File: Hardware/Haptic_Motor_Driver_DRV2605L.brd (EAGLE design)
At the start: 20.3 x 21.6 mm, 15 parts, among them U1 DRV2605L

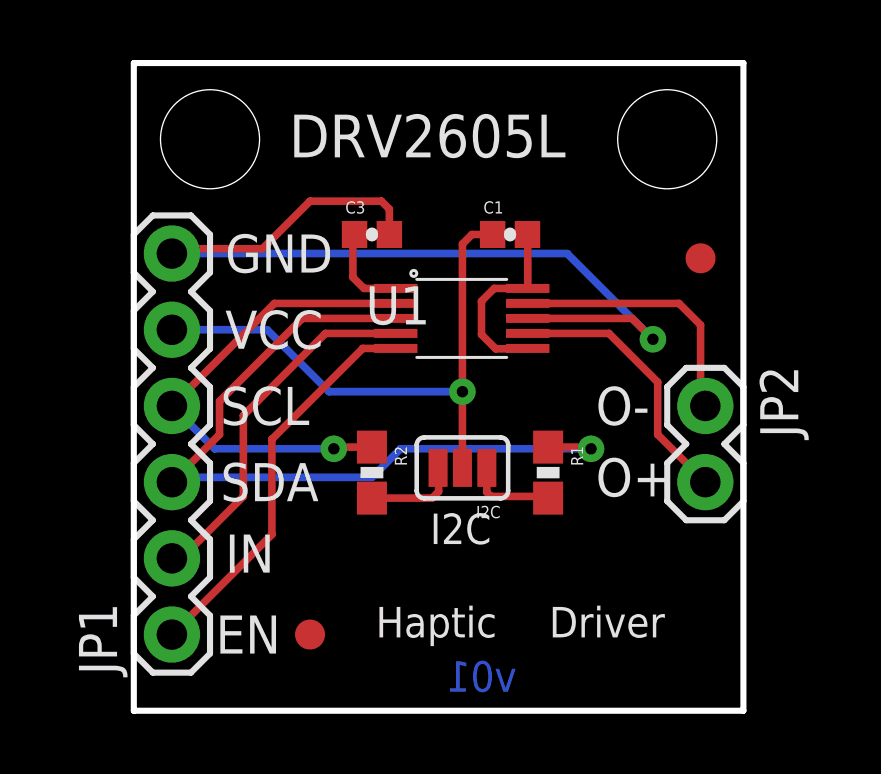
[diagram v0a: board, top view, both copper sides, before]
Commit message: Updated Per QC Checklist -- Switched SDA/SCL
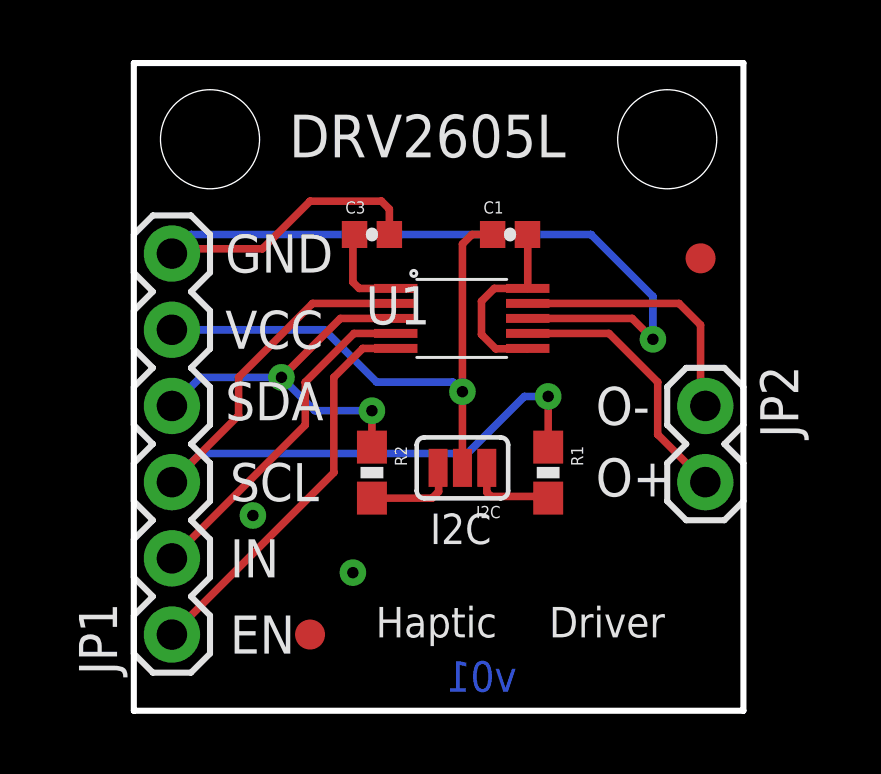
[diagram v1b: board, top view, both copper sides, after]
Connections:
- net N$1: now also U1.P$3; no longer U1.P$2
- net N$2: now also U1.P$2; no longer U1.P$3
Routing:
- net N$1: track 16.2 -> 13.4 mm, vias 1 -> 2
- net GND: track 30.6 -> 32.0 mm, vias 1 -> 3
- net N$4: track 12.1 -> 11.4 mm
